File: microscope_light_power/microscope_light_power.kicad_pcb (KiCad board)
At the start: 2 copper layers, 36 parts, among them IC1 TPS61090, J1 MICROUSB, J2 5V175_out, J3 enable_switch, U1 MCP73871-2AA

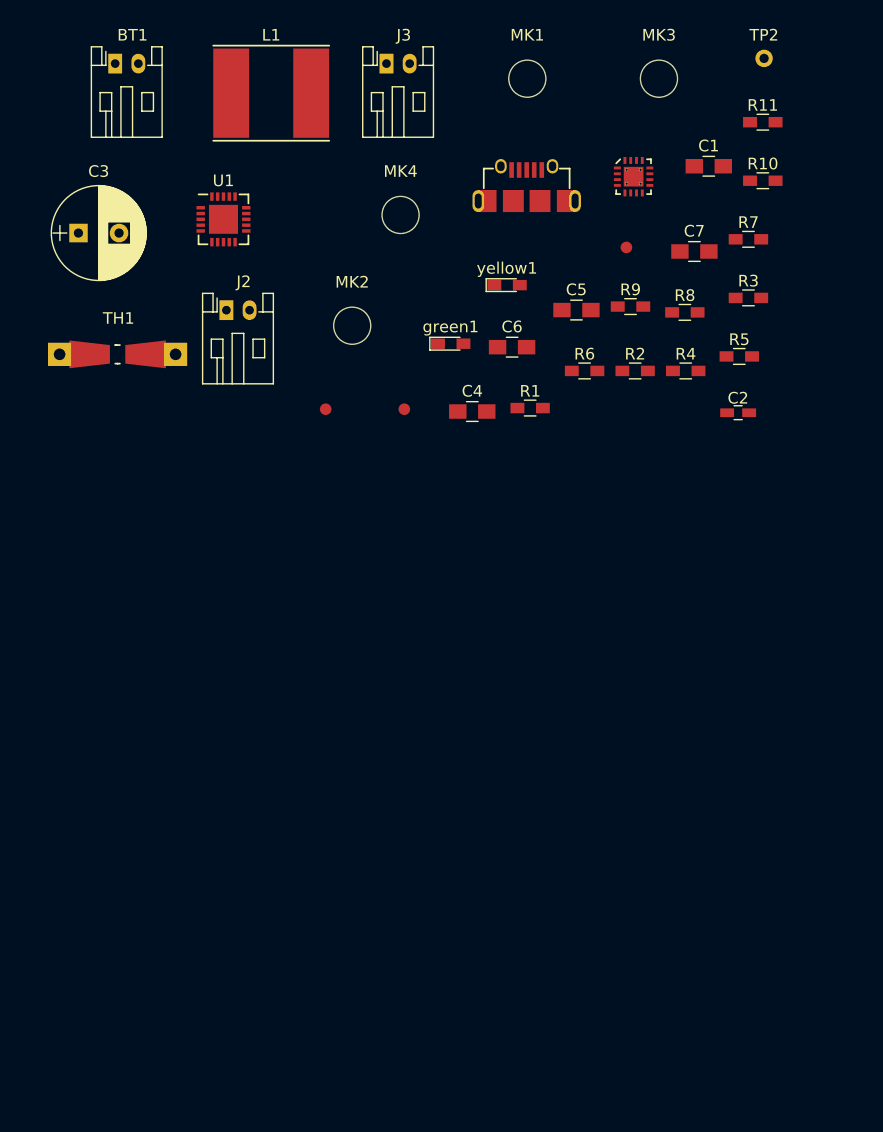
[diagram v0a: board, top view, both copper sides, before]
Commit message: Added a 40mm x 70mm board layout.
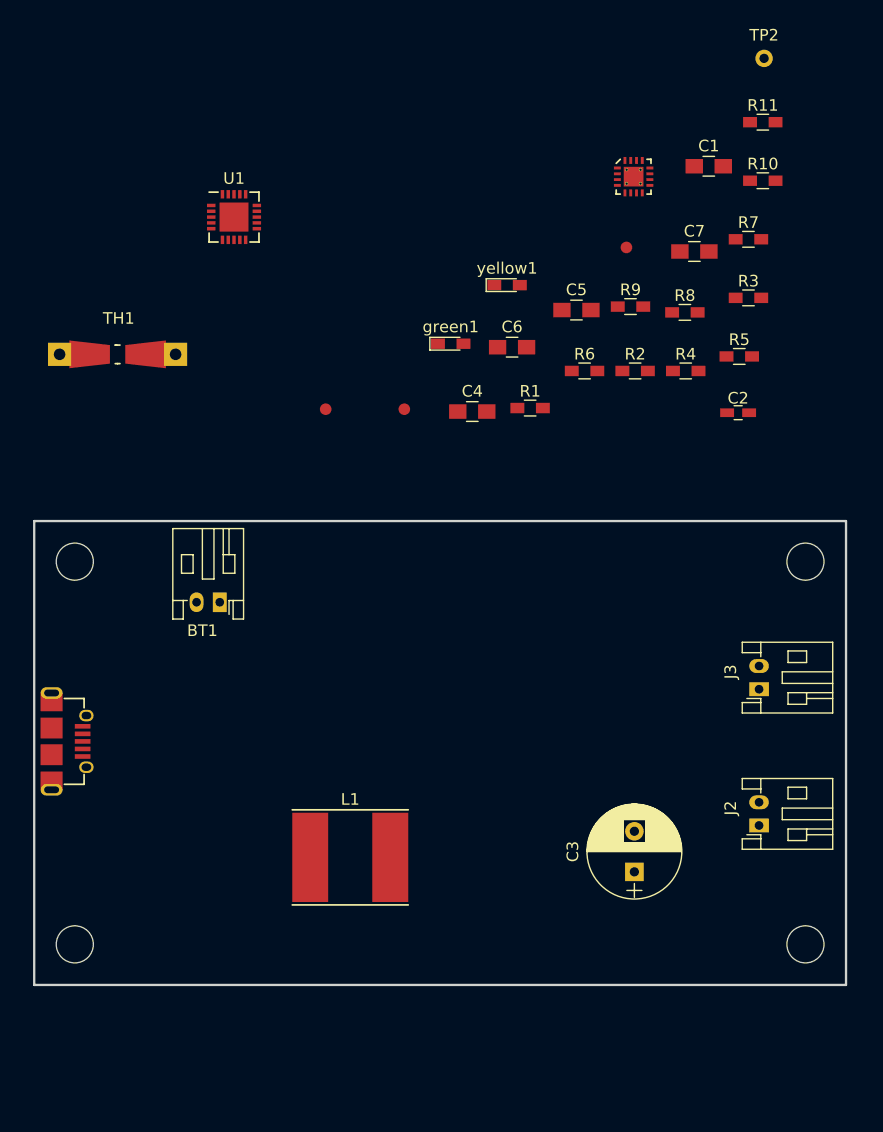
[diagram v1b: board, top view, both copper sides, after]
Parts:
- moved MK3 75.7 mm to (166.5, 156.5)
- moved C3 73.0 mm to (151.8, 150.2), turned to 90 degrees
- moved L1 66.2 mm to (127.2, 149.0)
- moved J2 63.9 mm to (162.5, 146.2), turned to 90 degrees
- moved J3 62.8 mm to (162.5, 134.5), turned to 90 degrees
- moved J1 62.0 mm to (101.5, 139.0), turned to 270 degrees
- moved MK2 58.5 mm to (103.5, 156.5)
- moved MK1 48.1 mm to (166.5, 123.5)
- moved BT1 47.3 mm to (116.0, 127.0), turned to 180 degrees
- moved MK4 41.0 mm to (103.5, 123.5)
- moved U1 0.93 mm to (117.2, 93.8)
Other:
- board outline added: 70 x 40 mm

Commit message: Arranged the components in a slightly more organized manner. This is mainly just to see how much room there is to work with and to get an idea of how the components should flow. Also added a gitignore for the extra backup files kicad generates.
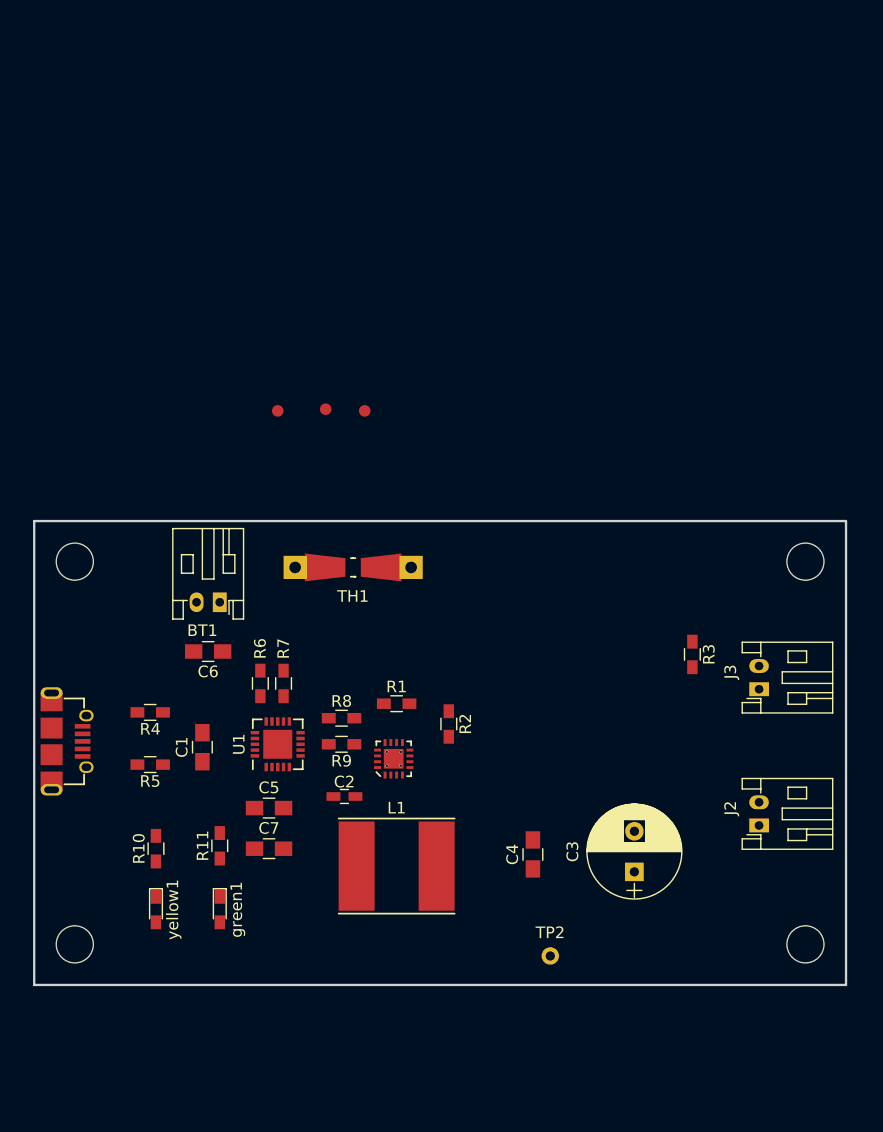
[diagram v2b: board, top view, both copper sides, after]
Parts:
- moved TP2 79.6 mm to (144.5, 157.5)
- moved R11 78.0 mm to (116.0, 148.0), turned to 90 degrees
- moved R10 77.8 mm to (110.5, 148.2), turned to 90 degrees
- moved C1 66.5 mm to (114.5, 139.5), turned to 90 degrees
- moved C7 63.2 mm to (120.2, 148.2)
- moved R5 61.8 mm to (110.0, 141.0), turned to 180 degrees
- moved yellow1 61.8 mm to (110.5, 153.5), turned to 270 degrees
- moved R7 55.4 mm to (121.5, 134.0), turned to 90 degrees
- moved R4 54.8 mm to (110.0, 136.5), turned to 180 degrees
- moved IC1 54.3 mm to (131.0, 140.5), turned to 90 degrees
- moved green1 52.7 mm to (116.0, 153.5), turned to 270 degrees
- moved C5 50.5 mm to (120.2, 144.8)
- moved C2 47.4 mm to (126.8, 143.8)
- moved R8 45.8 mm to (126.5, 137.0)
- moved U1 45.6 mm to (121.0, 139.2), turned to 90 degrees
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
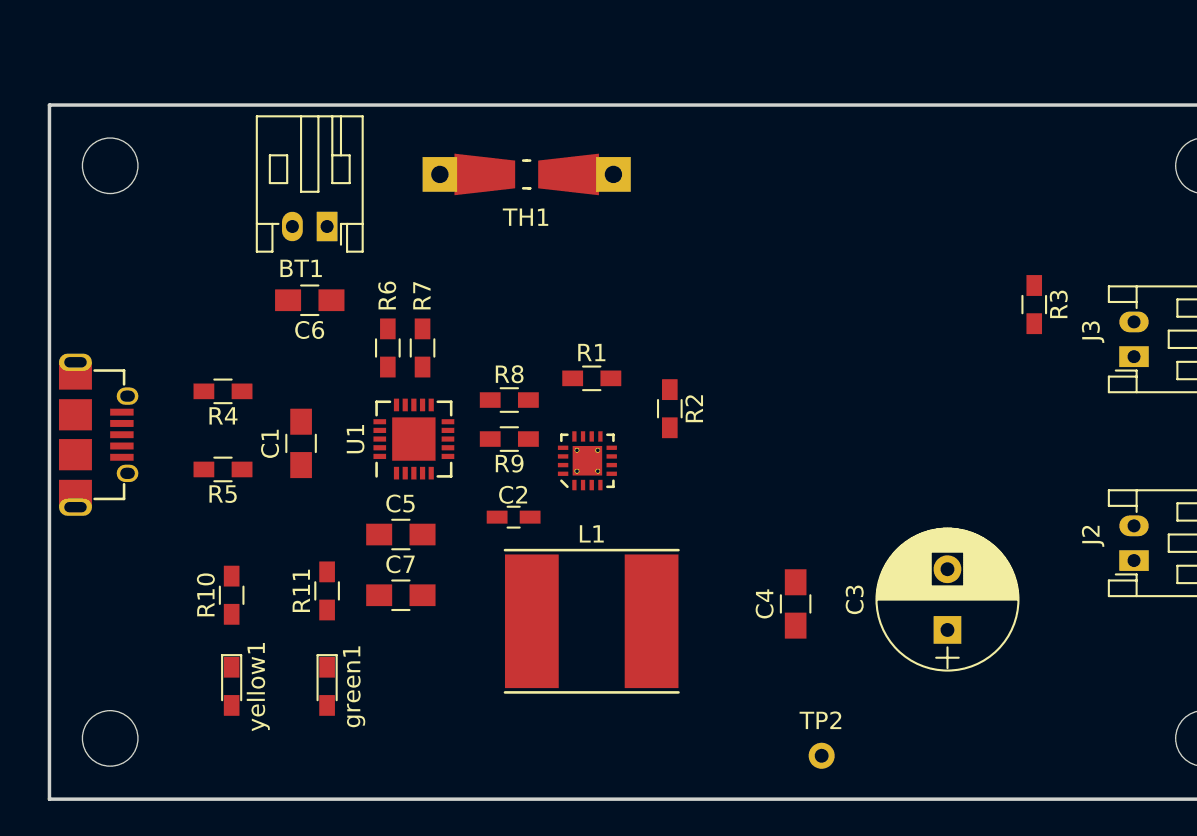
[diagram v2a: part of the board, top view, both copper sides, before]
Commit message: Put the parts for the MCP73871 battery charger in better locations. Some labeling was also placed to make sure the board can be used without looking at the schematic every time!
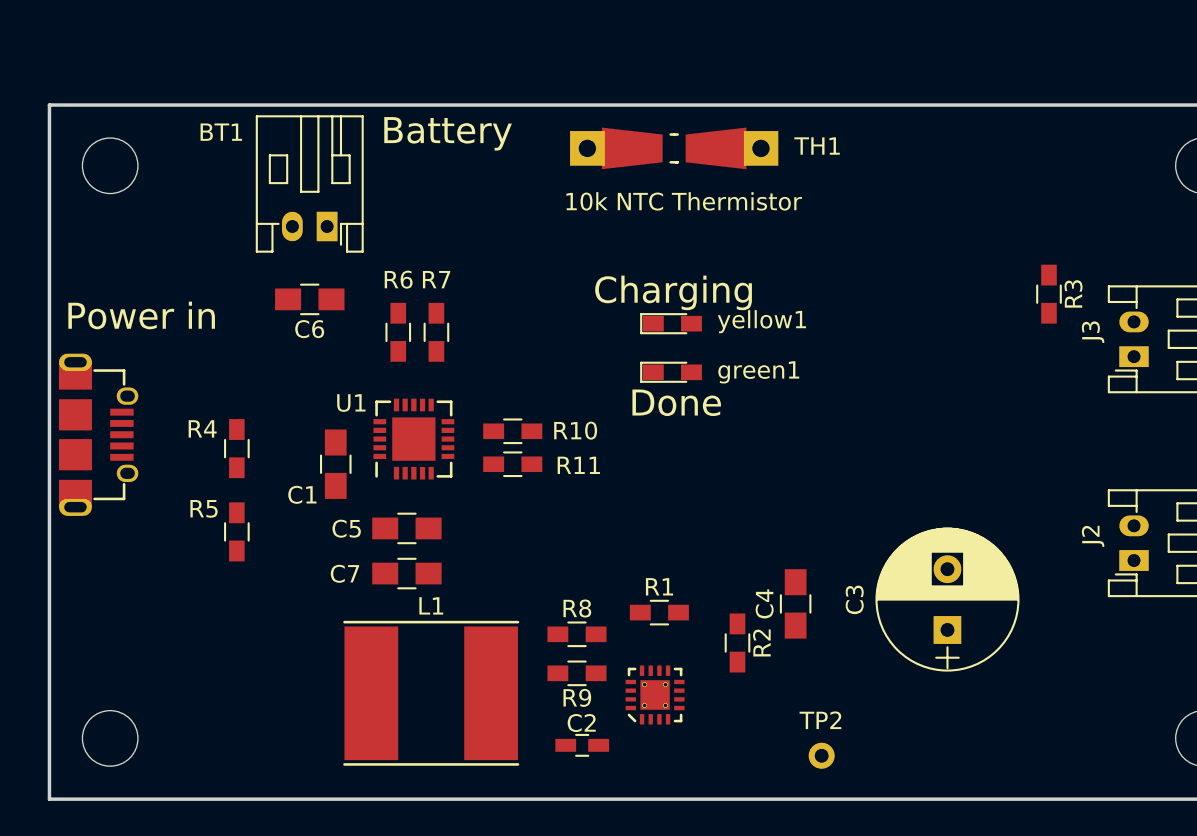
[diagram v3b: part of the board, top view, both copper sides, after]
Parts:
- moved yellow1 32.9 mm to (135.9, 132.6), turned to 0 degrees
- moved green1 26.9 mm to (135.9, 135.4), turned to 0 degrees
- moved R10 18.8 mm to (126.7, 138.8), turned to 180 degrees
- moved IC1 14.1 mm to (134.9, 154.0)
- moved R1 14.1 mm to (135.2, 149.2)
- moved R2 14.1 mm to (139.7, 151.0)
- moved R8 14.1 mm to (130.4, 150.5)
- moved R9 14.1 mm to (130.4, 152.8)
- moved C2 13.7 mm to (130.7, 156.9)
- moved R11 13.0 mm to (126.7, 140.7), turned to 180 degrees
- moved L1 10.1 mm to (122.0, 153.9)
- moved TH1 8.63 mm to (136.0, 122.5)
- moved R5 3.69 mm to (110.8, 144.6), turned to 270 degrees
- moved R4 3.40 mm to (110.8, 139.8), turned to 90 degrees
- moved C1 2.33 mm to (116.5, 140.7), turned to 270 degrees
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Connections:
- net Net-(IC1-Pad3) renamed /SW
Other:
- net class Default: clearance 0.2 -> 0.15
- rule trace_clearance: 0.2 -> 0.15
- rule trace_min: 0.2 -> 0.15
- board text added: "10k NTC Thermistor"
- board text added: "Battery"
- board text added: "Charging"
- board text added: "Done"
- board text added: "Power in"

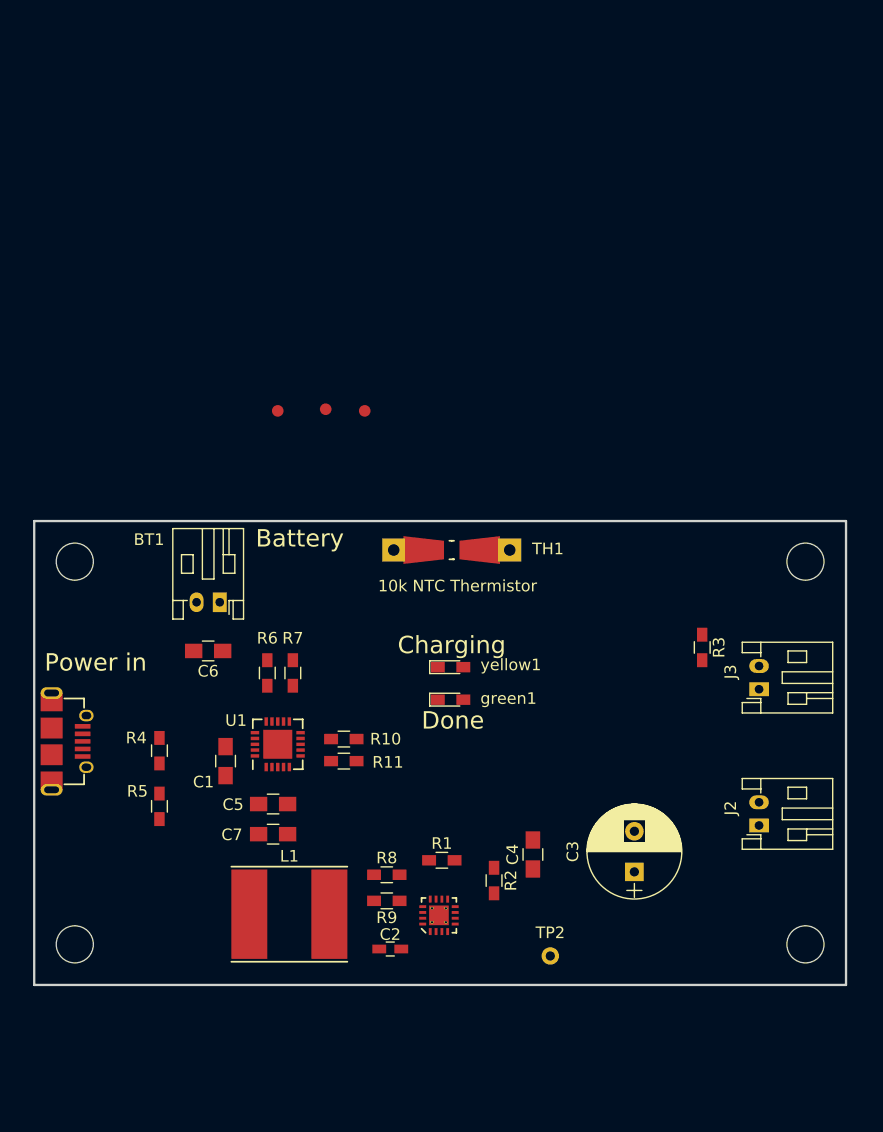
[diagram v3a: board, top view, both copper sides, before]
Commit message: After getting most things organized I saw that we can do better! Reduced the board length from 70mm to 50mm and started rearranging components to fit.
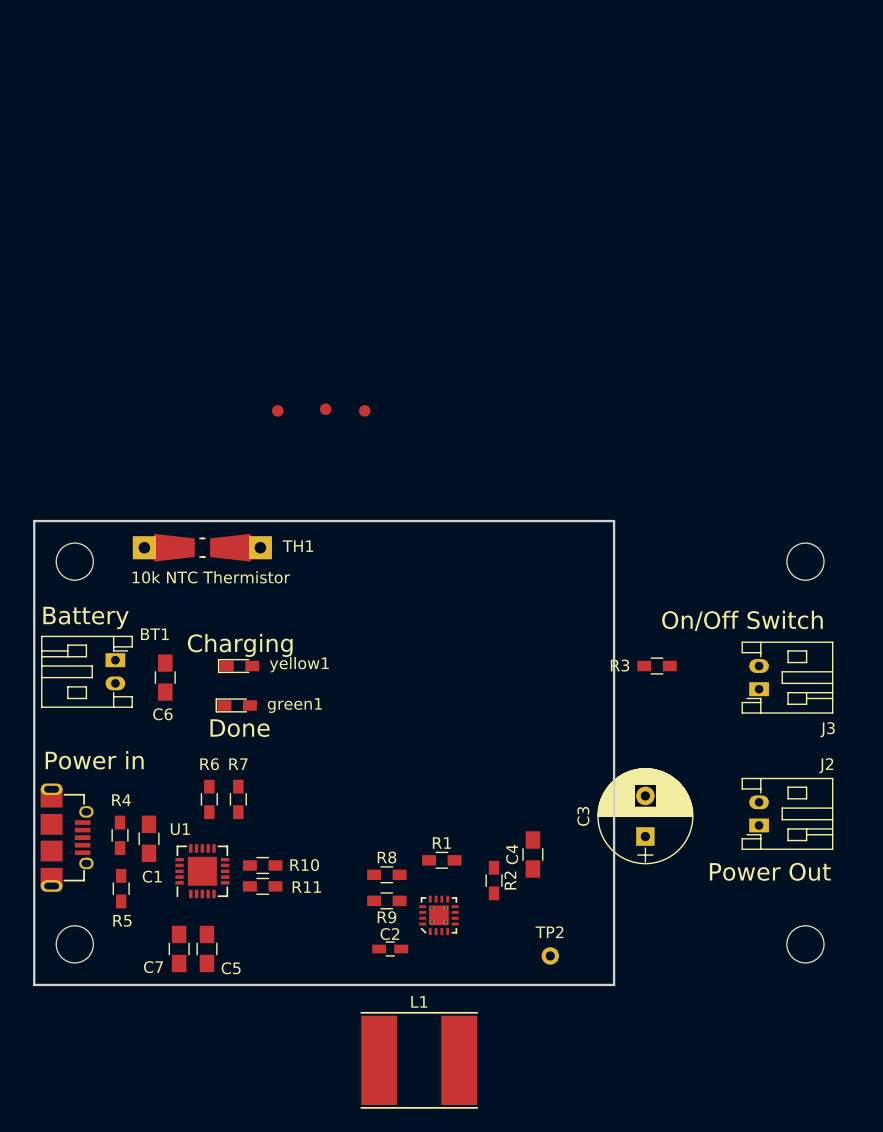
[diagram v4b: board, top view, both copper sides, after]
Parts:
- moved TH1 21.5 mm to (114.5, 122.3)
- moved green1 18.4 mm to (117.5, 135.9)
- moved yellow1 18.2 mm to (117.7, 132.5)
- moved L1 16.9 mm to (133.2, 166.5)
- moved C5 13.7 mm to (114.9, 156.9), turned to 270 degrees
- moved R10 13.0 mm to (119.7, 149.7)
- moved R11 12.9 mm to (119.7, 151.5)
- moved C7 12.8 mm to (112.5, 156.9), turned to 270 degrees
- moved U1 12.7 mm to (114.5, 150.2)
- moved R6 12.0 mm to (115.1, 144.0)
- moved R7 11.9 mm to (117.6, 144.0)
- moved BT1 10.3 mm to (107.0, 132.0), turned to 270 degrees
- moved C1 9.40 mm to (109.9, 147.4)
- moved J1 8.30 mm to (101.5, 147.3)
- moved R4 8.05 mm to (107.4, 147.1)
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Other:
- board size 70 x 40 mm -> 50 x 40 mm
- board text added: "On/Off Switch"
- board text added: "Power Out"

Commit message: Getting closer to a reasonable arrangement of components.
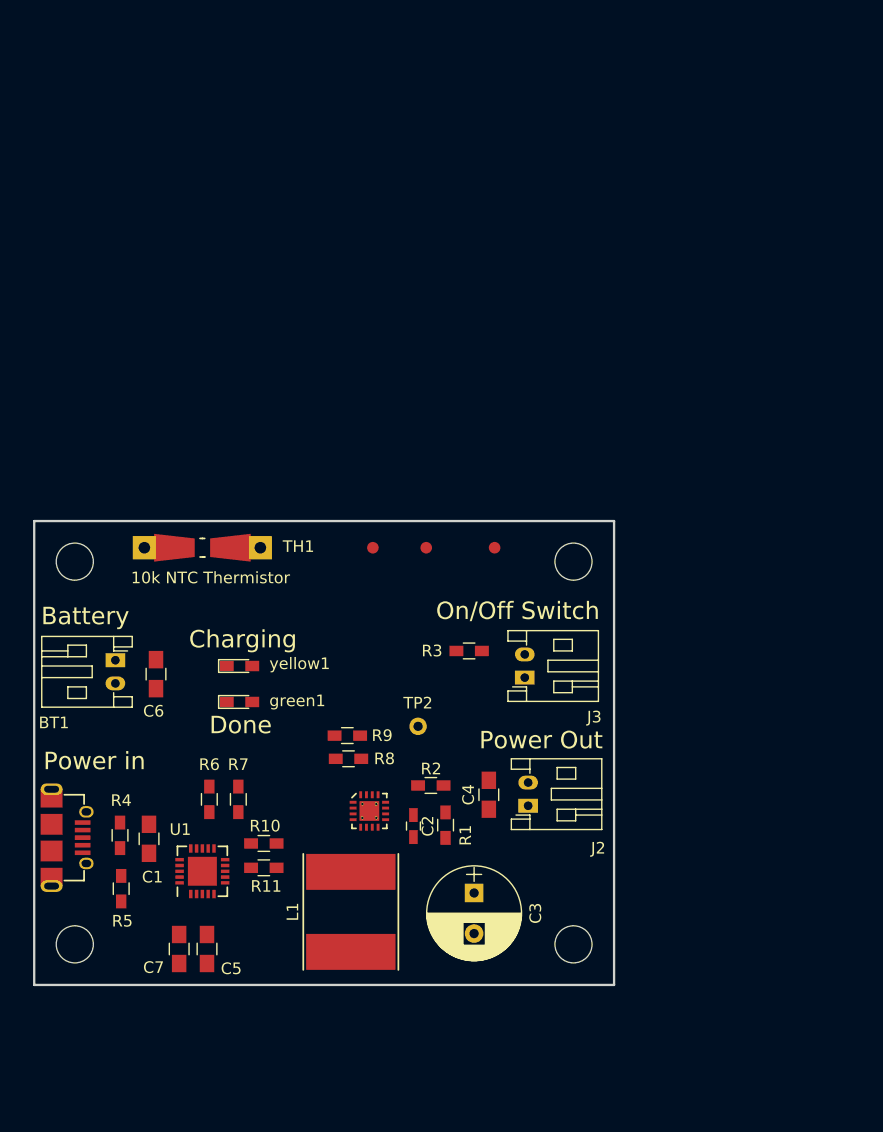
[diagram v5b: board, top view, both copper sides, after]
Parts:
- moved TP2 22.8 mm to (133.1, 137.7)
- moved TP4 22.1 mm to (139.7, 122.3)
- moved J3 20.2 mm to (142.3, 133.5)
- moved MK1 20.0 mm to (146.5, 123.5)
- moved MK3 20.0 mm to (146.5, 156.5)
- moved J2 20.0 mm to (142.6, 144.6)
- moved R3 16.3 mm to (137.5, 131.2)
- moved C3 15.6 mm to (137.9, 152.1), turned to 270 degrees
- moved TP3 14.8 mm to (133.8, 122.3)
- moved R9 14.7 mm to (127.0, 138.5)
- moved L1 14.1 mm to (127.3, 153.7), turned to 90 degrees
- moved TP1 11.8 mm to (129.2, 122.3)
- moved IC1 10.8 mm to (128.9, 145.0), turned to 0 degrees
- moved C2 10.8 mm to (132.7, 146.3), turned to 270 degrees
- moved R8 10.5 mm to (127.1, 140.5)
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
